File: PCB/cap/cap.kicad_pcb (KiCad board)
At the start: 2 copper layers, 21 parts, among them J1 Servo1, J2 Servo2, J3 LS1, J4 LS2, J5 VCC/GND-IN, J6 Radio, J7 FSR1, J8 FSR2, Q1 Q_PMOS_DGS, U1 ACS723xLCTR-05AB

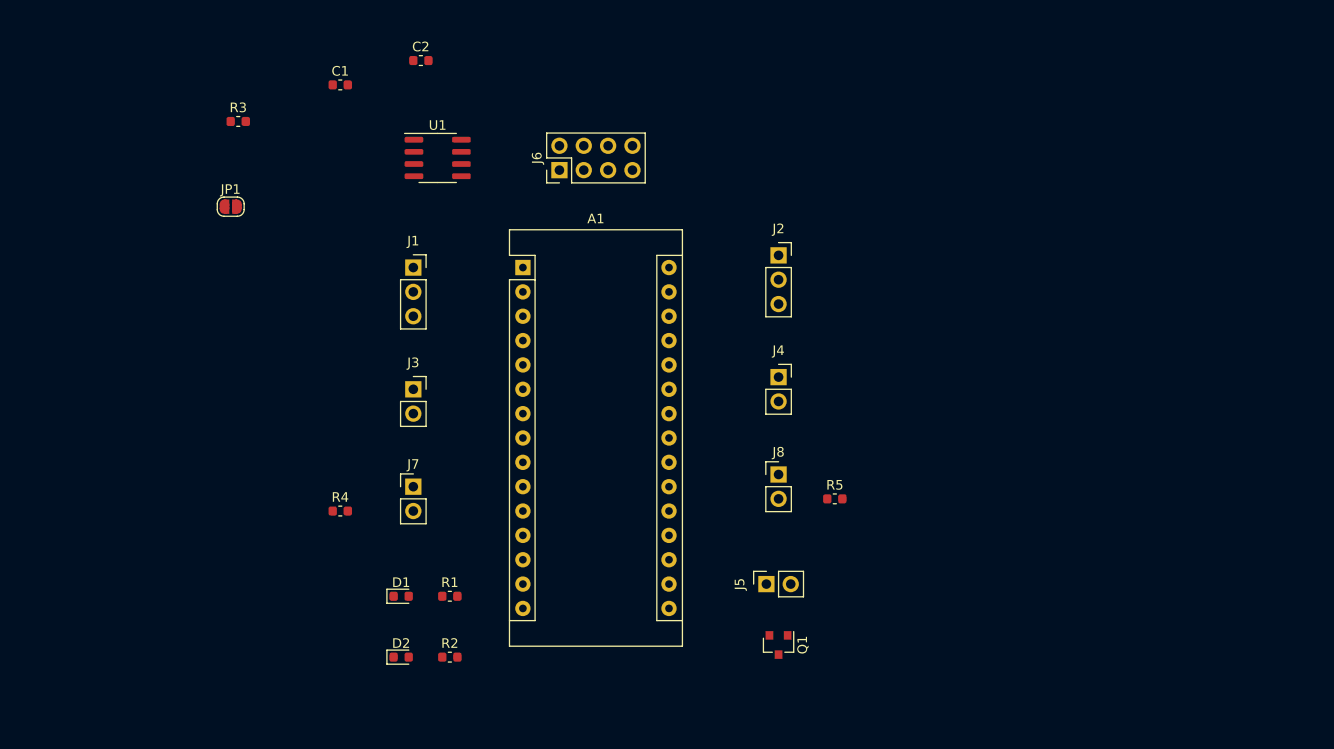
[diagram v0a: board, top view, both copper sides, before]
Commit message: Layout board ready for autorouting.
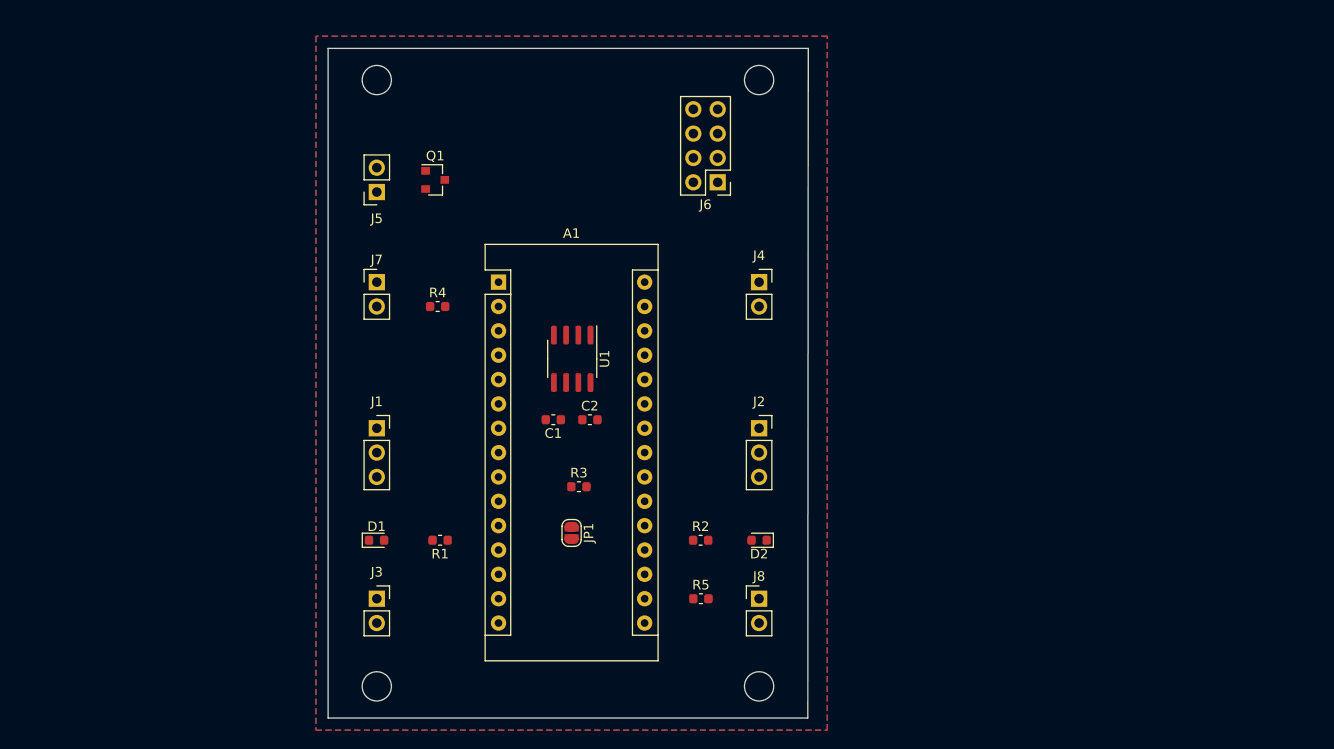
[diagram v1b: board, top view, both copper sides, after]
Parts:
- moved Q1 60.3 mm to (119.1, 59.4), turned to 0 degrees
- moved J5 57.7 mm to (113.0, 60.7), turned to 180 degrees
- moved R3 52.1 mm to (134.1, 91.4)
- moved JP1 49.2 mm to (133.3, 96.3), turned to 270 degrees
- moved C2 41.4 mm to (135.3, 84.5)
- moved C1 41.4 mm to (131.4, 84.5), turned to 180 degrees
- moved D2 39.3 mm to (152.9, 97.0), turned to 180 degrees
- moved R2 28.9 mm to (146.8, 97.0)
- moved U1 25.2 mm to (133.4, 78.1), turned to 270 degrees
- moved R4 23.6 mm to (119.4, 72.6)
- moved J3 22.2 mm to (113.0, 103.1)
- moved J7 21.7 mm to (113.0, 70.1)
- moved J2 18.1 mm to (152.9, 85.3)
- moved R5 17.4 mm to (146.8, 103.1)
- moved J1 17.2 mm to (113.0, 85.3)
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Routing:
- added copper zone on B.Cu, net GND
- added copper zone on F.Cu, net GND
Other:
- board outline added: 50.1 x 69.8 mm

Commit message: Minor updates to PCB. Push to windows.
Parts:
- removed J2: Servo2, Connector_PinSocket_2.54mm:PinSocket_1x03_P2.54mm_Vertical
- removed J8: FSR2, Connector_PinHeader_2.54mm:PinHeader_1x02_P2.54mm_Vertical
- removed R5: 10k, Resistor_SMD:R_0603_1608Metric
- added U2: NRF24L01_Breakout, RF_Module:nRF24L01_Breakout, F.Cu at (127.0, 49.3)
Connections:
- A1 pad 21: A2 -> Net-(A1-Pad21)
- C1 pad 1: A2 -> A1
- J1 pad 2: Vdrive -> VCC
- J5 pad 2: Net-(J5-Pad2) -> VCC
- U1 pad 3: Vdrive -> VCC
- U1 pad 4: Vdrive -> VCC
- U1 pad 7: A2 -> A1
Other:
- outline, holes or cut-outs redrawn

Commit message: Conceptual schematic completed
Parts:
- removed J6: Radio, Connector_PinHeader_2.54mm:PinHeader_2x04_P2.54mm_Vertical
- removed Q1: Q_PMOS_DGS, Package_TO_SOT_SMD:SOT-23
- added C3: 0.1 uF, Capacitor_SMD:C_0603_1608Metric, F.Cu at (199.3, 64.0)
- added H1: MountingHole_Pad, MountingHole:MountingHole_3.2mm_M3_ISO14580_Pad, F.Cu at (151.4, 50.0)
- added H2: MountingHole_Pad, MountingHole:MountingHole_3.2mm_M3_ISO14580_Pad, F.Cu at (114.0, 50.3)
- added H3: MountingHole_Pad, MountingHole:MountingHole_3.2mm_M3_ISO14580_Pad, F.Cu at (113.8, 105.4)
- added H4: MountingHole_Pad, MountingHole:MountingHole_3.2mm_M3_ISO14580_Pad, F.Cu at (150.6, 105.7)
- added R5: -, Resistor_SMD:R_0603_1608Metric_Pad1.05x0.95mm_HandSolder, F.Cu at (194.3, 64.4)
- added U3: INA181A3, Package_TO_SOT_SMD:SOT-23-6, F.Cu at (178.6, 53.3)
- D1: footprint LED_SMD:LED_0603_1608Metric -> LED_SMD:LED_0603_1608Metric_Pad1.05x0.95mm_HandSolder
- D2: value R-LED -> G-LED; footprint LED_SMD:LED_0603_1608Metric -> LED_SMD:LED_0603_1608Metric_Pad1.05x0.95mm_HandSolder
- R1: value 140 -> 16 mOhm; footprint Resistor_SMD:R_0603_1608Metric -> Resistor_SMD:R_2512_6332Metric_Pad1.52x3.35mm_HandSolder
- R2: value 140 -> -; footprint Resistor_SMD:R_0603_1608Metric -> Resistor_SMD:R_0603_1608Metric_Pad1.05x0.95mm_HandSolder
- R3: value 5.1K -> 5.1 kOhm
- R4: value 10k -> 10 kOhm
- moved C1 75.6 mm to (205.9, 97.7)
- moved C2 75.6 mm to (209.7, 97.7)
- moved JP1 75.6 mm to (207.8, 109.5)
- moved R3 75.6 mm to (208.5, 104.6)
- moved R1 69.9 mm to (178.6, 59.4), turned to 0 degrees
- moved J4 47.6 mm to (198.1, 84.8)
- moved R2 47.6 mm to (192.0, 111.8)
- moved U1 46.6 mm to (179.5, 70.9), turned to 0 degrees
- moved R4 39.1 mm to (80.3, 71.6)
- moved J5 36.1 mm to (77.5, 66.8)
- moved J7 36.1 mm to (77.5, 76.2)
- moved J1 35.6 mm to (77.5, 85.3)
- moved J3 35.6 mm to (77.5, 103.1)
- moved D1 35.6 mm to (77.4, 97.0)
- moved D2 33.1 mm to (178.3, 75.8), turned to 0 degrees
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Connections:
- A1 pad 1: Net-(A1-Pad1) -> (no net)
- A1 pad 13: D13 -> (no net)
- A1 pad 18: Net-(A1-Pad18) -> (no net)
- A1 pad 2: Net-(A1-Pad2) -> (no net)
- A1 pad 21: Net-(A1-Pad21) -> A2
- A1 pad 22: Net-(A1-Pad22) -> (no net)
- A1 pad 23: Net-(A1-Pad23) -> (no net)
- A1 pad 24: Net-(A1-Pad24) -> (no net)
- A1 pad 25: Net-(A1-Pad25) -> (no net)
- A1 pad 26: Net-(A1-Pad26) -> (no net)
- A1 pad 28: Net-(A1-Pad28) -> (no net)
- A1 pad 3: Net-(A1-Pad3) -> (no net)
- A1 pad 8: D5 -> (no net)
- A1 pad 9: Net-(A1-Pad9) -> (no net)
- J1 pad 2: VCC -> Vdrive
- R1 pad 1: D9 -> Vdrive
- R1 pad 2: Net-(D1-Pad2) -> Vdrive
- R2 pad 1: D10 -> (no net)
- U1 pad 3: VCC -> Vdrive
- U1 pad 4: VCC -> Vdrive
- U2 pad 1: Net-(U2-Pad1) -> GND
- U2 pad 2: Net-(U2-Pad2) -> +3V3
- U2 pad 3: Net-(U2-Pad3) -> CE
- U2 pad 4: Net-(U2-Pad4) -> CSN
- U2 pad 5: Net-(U2-Pad5) -> SCK
- U2 pad 6: Net-(U2-Pad6) -> MOSI
- U2 pad 7: Net-(U2-Pad7) -> MISO
- U2 pad 8: Net-(U2-Pad8) -> (no net)
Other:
- board size 50.1 x 69.8 mm -> 45 x 65 mm

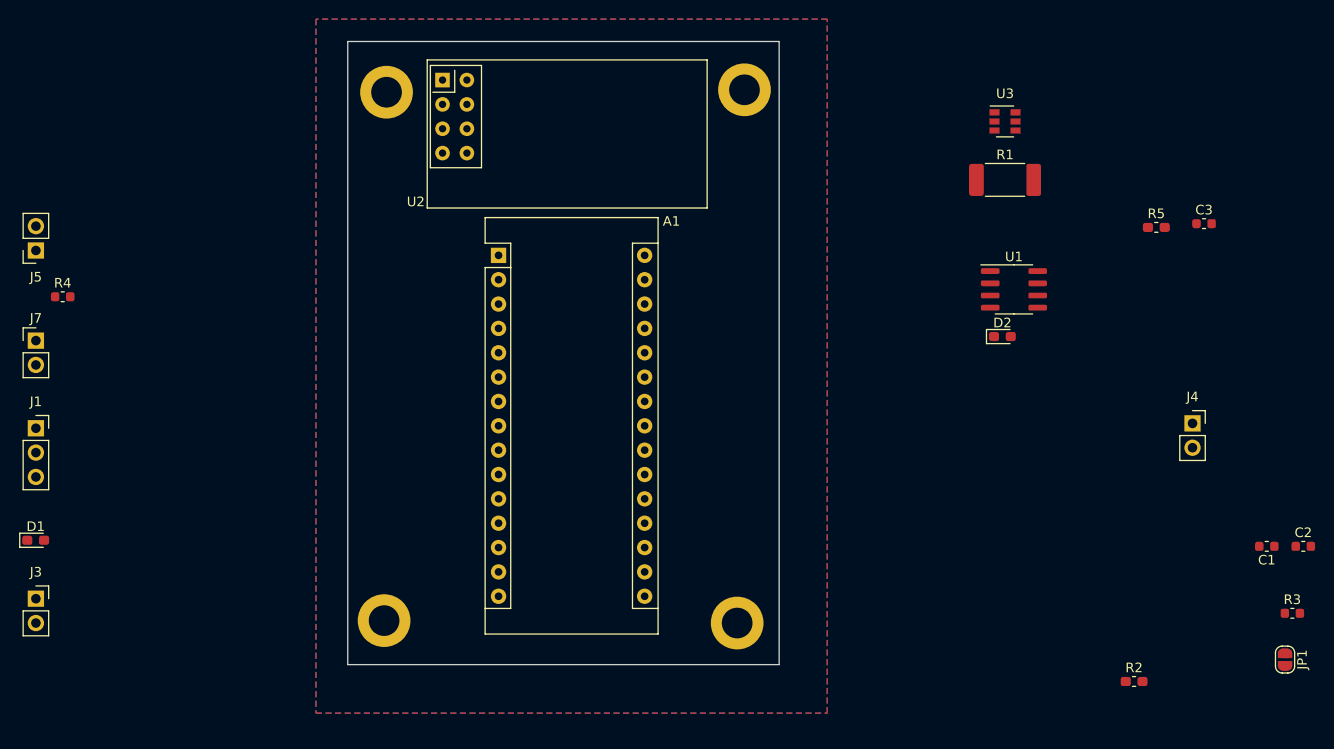
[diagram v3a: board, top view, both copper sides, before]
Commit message: Layed out mjaor components, need to select connectors.
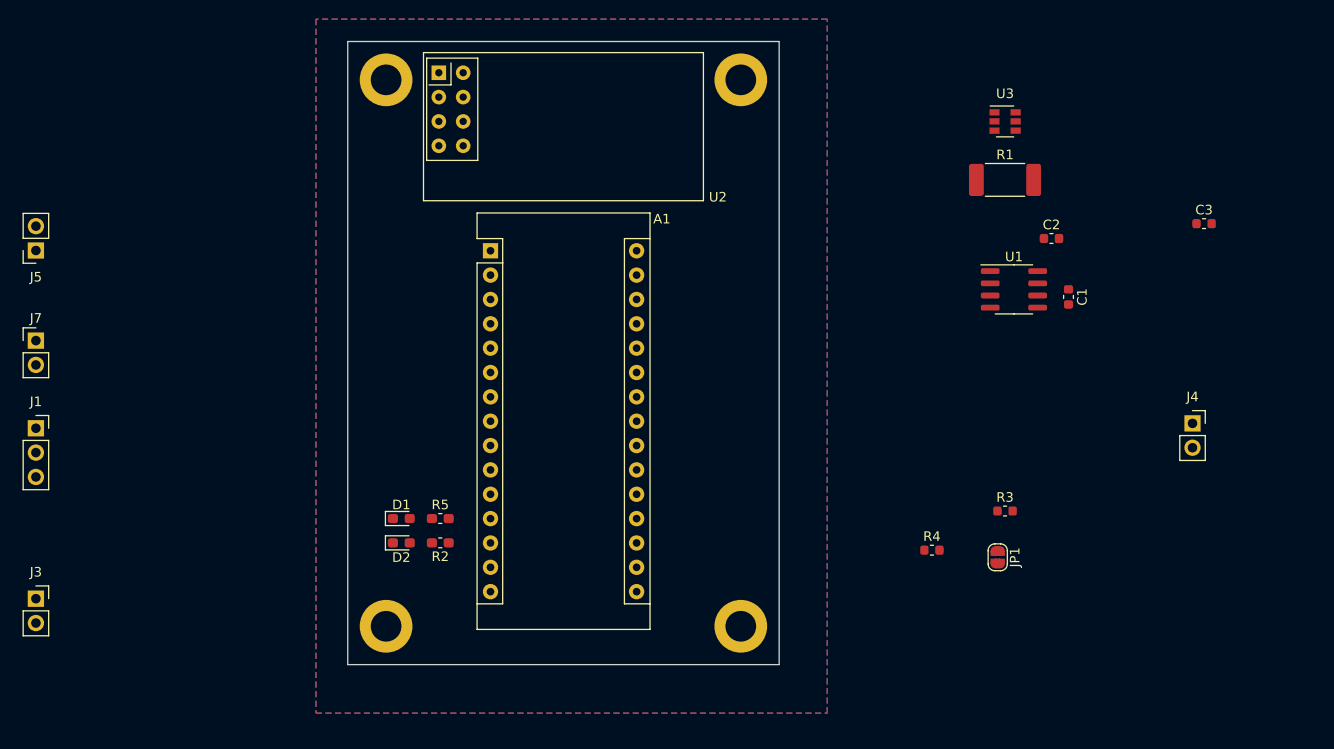
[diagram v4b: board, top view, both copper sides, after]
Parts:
- moved R4 94.4 mm to (170.9, 98.1)
- moved R5 80.6 mm to (119.7, 94.8)
- moved R2 73.8 mm to (119.7, 97.3), turned to 180 degrees
- moved D2 66.3 mm to (115.6, 97.3)
- moved C2 41.5 mm to (183.4, 65.5)
- moved D1 38.2 mm to (115.6, 94.8)
- moved C1 33.2 mm to (185.2, 71.6), turned to 270 degrees
- moved JP1 31.8 mm to (177.8, 98.8)
- moved R3 31.8 mm to (178.6, 94.0)
- moved H2 1.29 mm to (114.0, 49.0)
- moved H1 1.11 mm to (151.0, 49.0)
- moved A1 0.97 mm to (124.9, 66.8)
- moved U2 0.86 mm to (119.5, 48.3)
- moved H3 0.63 mm to (114.0, 106.0)
- moved H4 0.51 mm to (151.0, 106.0)
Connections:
- A1 pad 13: (no net) -> D10
- R2 pad 1: (no net) -> D10
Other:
- net class Default: trace_width 0.25 -> 0.381

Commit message: Added Molex connectors and conceptual layout complete
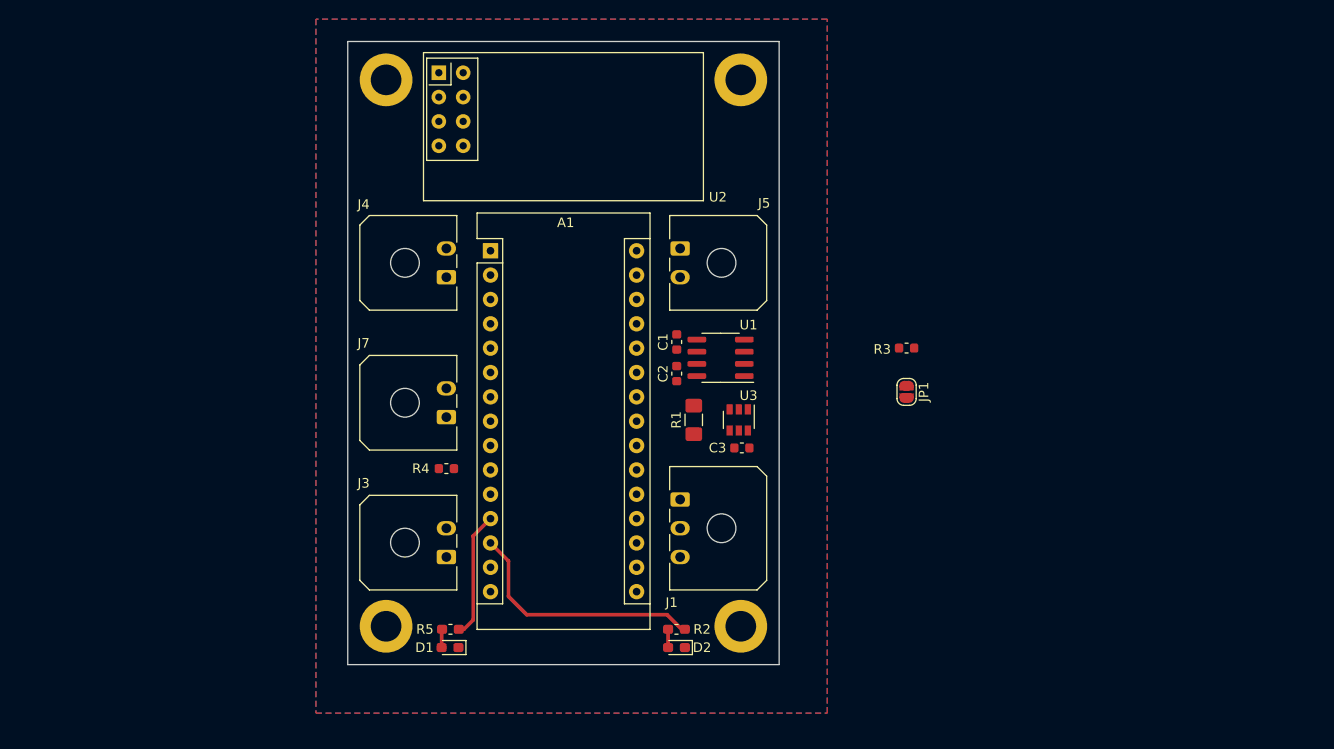
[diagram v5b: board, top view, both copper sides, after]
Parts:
- J1: footprint Connector_PinSocket_2.54mm:PinSocket_1x03_P2.54mm_Vertical -> Connector_Molex:Molex_Micro-Fit_3.0_43650-0300_1x03_P3.00mm_Horizontal
- J3, J4, J5: footprint Connector_PinSocket_2.54mm:PinSocket_1x02_P2.54mm_Vertical -> Connector_Molex:Molex_Micro-Fit_3.0_43650-0200_1x02_P3.00mm_Horizontal
- J7: footprint Connector_PinHeader_2.54mm:PinHeader_1x02_P2.54mm_Vertical -> Connector_Molex:Molex_Micro-Fit_3.0_43650-0200_1x02_P3.00mm_Horizontal
- R1: footprint Resistor_SMD:R_2512_6332Metric_Pad1.52x3.35mm_HandSolder -> Resistor_SMD:R_1206_3216Metric_Pad1.42x1.75mm_HandSolder
- moved J4 79.3 mm to (120.3, 69.6), turned to 90 degrees
- moved J1 67.6 mm to (144.7, 92.8), turned to 270 degrees
- moved J5 67.2 mm to (144.7, 66.6), turned to 270 degrees
- moved C3 53.6 mm to (151.1, 87.4), turned to 180 degrees
- moved R4 51.4 mm to (120.3, 89.6)
- moved J7 43.6 mm to (120.3, 84.2), turned to 90 degrees
- moved J3 43.0 mm to (120.3, 98.8), turned to 90 degrees
- moved U3 41.7 mm to (150.8, 84.5), turned to 270 degrees
- moved C2 41.6 mm to (144.3, 79.6), turned to 90 degrees
- moved C1 41.1 mm to (144.3, 76.3), turned to 90 degrees
- moved R1 41.0 mm to (146.1, 84.5), turned to 90 degrees
- moved U1 31.4 mm to (148.9, 78.0), turned to 180 degrees
- moved D2 30.7 mm to (144.3, 108.2), turned to 180 degrees
- moved R2 26.2 mm to (144.3, 106.3)
- moved R3 19.9 mm to (168.3, 77.0)
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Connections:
- A1 pad 20: A1 -> (no net)
- A1 pad 25: (no net) -> A6
- C1 pad 1: A1 -> A6
- J1 pad 1: D4 -> GND
- J1 pad 3: GND -> D4
- J3 pad 1: D2 -> GND
- J3 pad 2: GND -> D2
- J4 pad 1: D3 -> GND
- J4 pad 2: GND -> D3
- J7 pad 1: +5V -> A0
- J7 pad 2: A0 -> +5V
- R1 pad 2: Vdrive -> VDD
- U1 pad 3: Vdrive -> VDD
- U1 pad 4: Vdrive -> VDD
- U1 pad 7: A1 -> A6
- U3 pad 3: Vdrive -> VDD
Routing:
- net D10: track 0.00 -> 26.2 mm
- net D9: track 0.00 -> 13.2 mm
- net Net-(D1-Pad2): track 0.00 -> 1.92 mm
- net Net-(D2-Pad2): track 0.00 -> 1.90 mm

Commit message: Board routed.
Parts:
- moved JP1 32.7 mm to (136.5, 73.9)
- moved R3 19.6 mm to (148.9, 74.4)
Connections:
- J3 pad 2: D2 -> D3
- J4 pad 2: D3 -> D2
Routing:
- net SCK: track 0.00 -> 74.8 mm
- net +5V: track 0.00 -> 70.0 mm, vias 0 -> 1
- net +3V3: track 0.00 -> 61.8 mm
- net MOSI: track 0.00 -> 50.3 mm
- net MISO: track 0.00 -> 48.7 mm
- net CSN: track 0.00 -> 44.8 mm
- net CE: track 0.00 -> 43.8 mm
- net D4: track 0.00 -> 29.1 mm
- net A0: track 0.00 -> 27.8 mm
- net VCC: track 0.00 -> 24.2 mm
- net D3: track 0.00 -> 23.1 mm
- net Vdrive: track 0.00 -> 16.6 mm
- net BW_SEL: track 0.00 -> 16.4 mm
- net VDD: track 0.00 -> 15.7 mm
- net A2: track 0.00 -> 14.7 mm
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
